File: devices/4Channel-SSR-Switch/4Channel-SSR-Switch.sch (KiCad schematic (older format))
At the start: 23 parts, among them J1 RJ45, J2 RJ45, P1 CONN_02X05, P2 CONN_01X05, P3 CONN_01X05, P4 CONN_01X05, P6 CONN_01X05, U1 LP2950, U2 STM32F030R8, U3 G3MB_SSR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

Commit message: Big cleanup/upgrade of Kicad files
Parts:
- added D1: SMF05C, SMF05C:SC70-6, symbol SMF05C:SMF05C
- added ZD1: DS9503, DS9503:TSOC6, symbol DS9503:DS9503
- C1: symbol CP -> 4Channel-SSR-Switch-rescue:CP
- C2, C3, C4, C5: symbol C -> 4Channel-SSR-Switch-rescue:C
- J1, J2: symbol RJ45 -> 4Channel-SSR-Switch-rescue:RJ45
- P1: symbol CONN_02X05 -> 4Channel-SSR-Switch-rescue:CONN_02X05
- P2, P3, P4, P6: symbol CONN_01X05 -> 4Channel-SSR-Switch-rescue:CONN_01X05
- R1: symbol R -> 4Channel-SSR-Switch-rescue:R
- RP1, RP2, RP3, RP4: symbol R_PACK4 -> 4Channel-SSR-Switch-rescue:R_PACK4
- U1: symbol LP2950 -> 4Channel-SSR-Switch-rescue:LP2950
- U2: symbol STM32F030R8 -> 4Channel-SSR-Switch-rescue:STM32F030R8
- U3, U4, U5, U6: symbol G3MB_SSR -> 4Channel-SSR-Switch-rescue:G3MB_SSR
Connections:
- net +5V: now also D1.1 (C1), D1.3 (C2), D1.4 (C3), D1.5 (C4), D1.6 (C5)
- net 1W-DATA: now also ZD1.1 (P$1); no longer J1.4, J2.4
- net GND: now also D1.2 (A), ZD1.2 (P$2); no longer J1.1, J1.3, J1.5, J1.8, J1.9 (SHIELD), J2.1, J2.3, J2.5, J2.8, J2.9 (SHIELD)
- new net: J1.1, J1.3, J1.5, J1.8, J1.9 (SHIELD), J2.1, J2.3, J2.5, J2.8, J2.9 (SHIELD), ZD1.5 (P$3)
- new net: J1.4, J2.4, ZD1.6 (P$4)

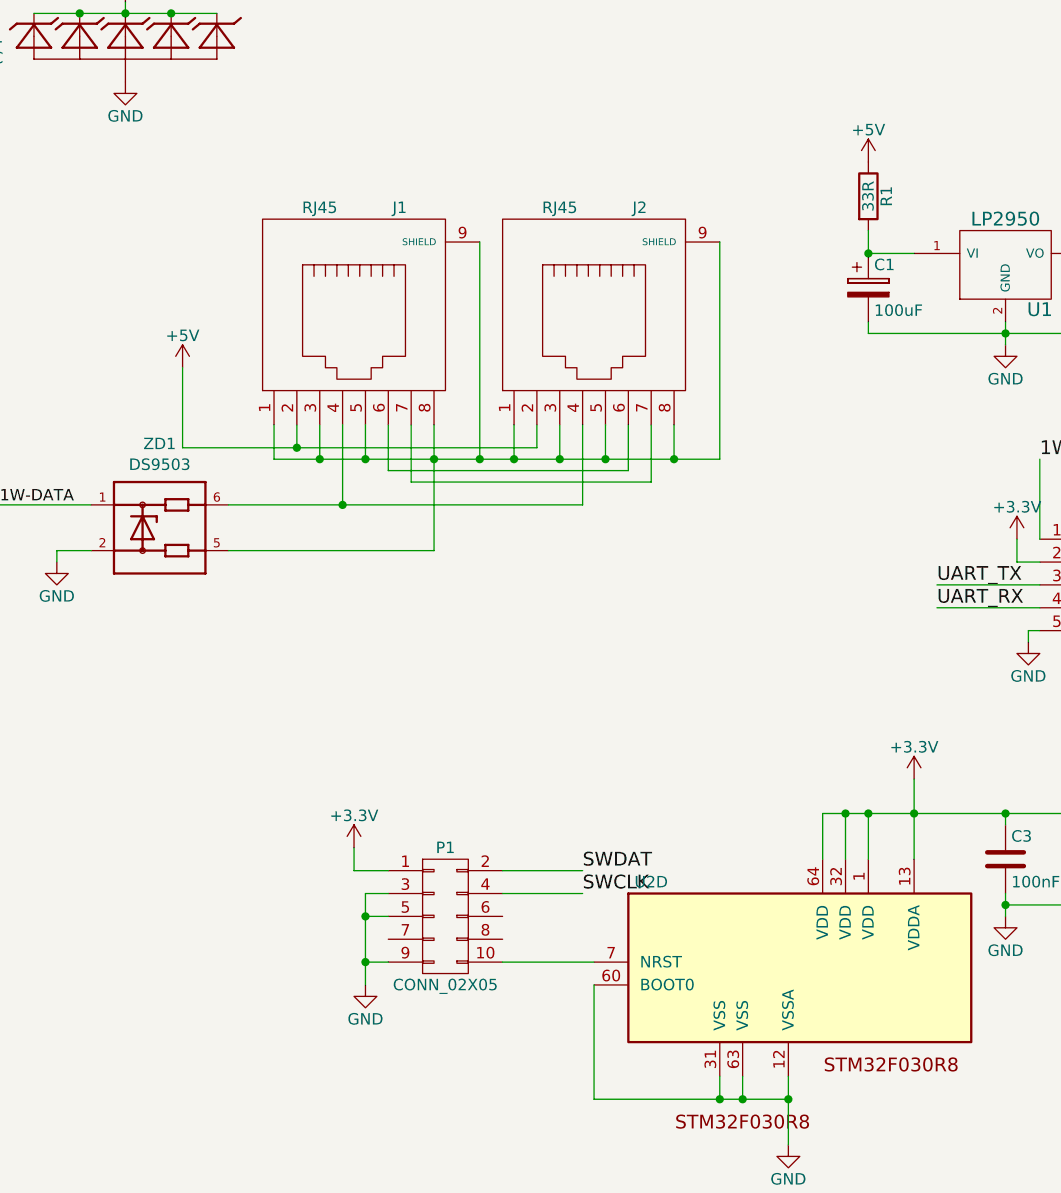
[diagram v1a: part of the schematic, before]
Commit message: Bump all active boards to Revision 1.2
- Remove dropping resistor from 5V power line
- Add pullup resistor to Reset line
- Add pin markings to STM32 chip footprint

Signed-off-by: Alastair D'Silva <alastair@d-silva.org>
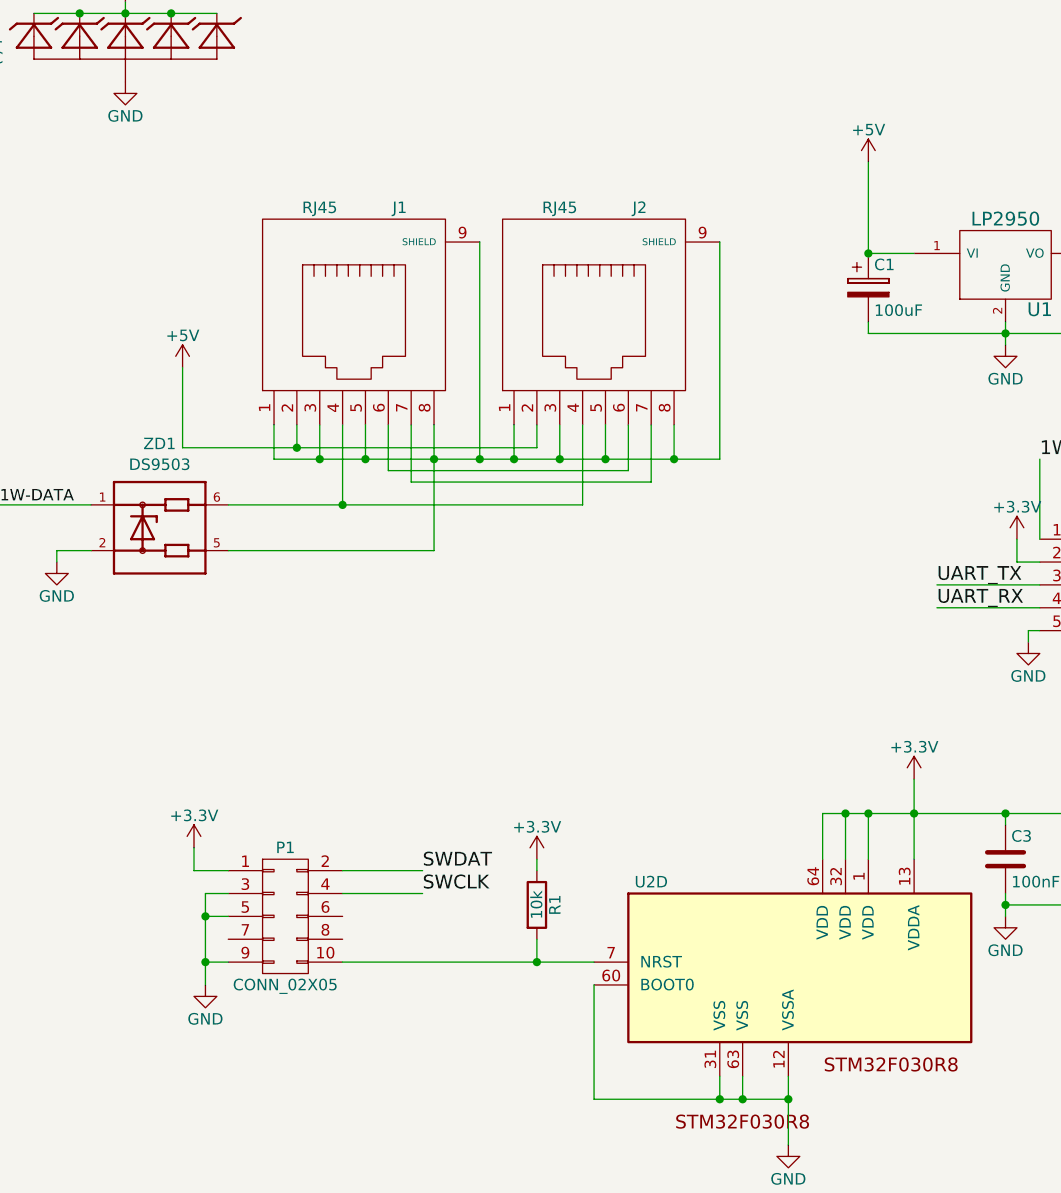
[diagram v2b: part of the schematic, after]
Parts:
- R1: value 33R -> 10k
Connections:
- net +3V3: now also R1.1
- net +5V: now also C1.1, U1.1 (VI); no longer R1.1
- net at P1.10 (P10), U2.7 (NRST): now also R1.2
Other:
- moved on the sheet: P1, R1
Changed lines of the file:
@@
 Sheet 1 1
 Title "4 Channel SSR Switch"
-Date "2018-10-30"
-Rev "1.0"
+Date "2018-12-23"
+Rev "1.2"
 Comp "Inferno Embedded"
 Comment1 "Licensed under the TAPR Open Hardware License (www.tapr.org/OHL)"
@@
 L 4Channel-SSR-Switch-rescue:CONN_02X05 P1
 U 1 1 58245605
-P 12450 8500
-F 0 "P1" H 12450 8800 50  0000 C CNN
-F 1 "CONN_02X05" H 12450 8200 50  0000 C CNN
-F 2 "Pin_Headers:Pin_Header_Straight_2x05_Pitch2.54mm_SMD" H 12450 7300 50  0001 C CNN
-F 3 "" H 12450 7300 50  0000 C CNN
-	1    12450 8500
+P 11750 8500
+F 0 "P1" H 11750 8800 50  0000 C CNN
+F 1 "CONN_02X05" H 11750 8200 50  0000 C CNN
+F 2 "Pin_Headers:Pin_Header_Straight_2x05_Pitch2.54mm_SMD" H 11750 7300 50  0001 C CNN
+F 3 "" H 11750 7300 50  0000 C CNN
+	1    11750 8500
 	1    0    0    -1
 $EndComp
@@
 L 4Channel-SSR-Switch-rescue:GND #PWR05
 U 1 1 58245733
-P 12100 8800
-F 0 "#PWR05" H 12100 8550 50  0001 C CNN
-F 1 "GND" H 12100 8650 50  0000 C CNN
-F 2 "" H 12100 8800 50  0000 C CNN
-F 3 "" H 12100 8800 50  0000 C CNN
-	1    12100 8800
+P 11400 8800
+F 0 "#PWR05" H 11400 8550 50  0001 C CNN
+F 1 "GND" H 11400 8650 50  0000 C CNN
+F 2 "" H 11400 8800 50  0000 C CNN
+F 3 "" H 11400 8800 50  0000 C CNN
+	1    11400 8800
 	1    0    0    -1
 $EndComp
@@
 F 3 "" H 5100 6850 50  0000 C CNN
 	5    1800 9350
-	1    0    0    -1
-$EndComp
-$Comp
-L 4Channel-SSR-Switch-rescue:R R1
-U 1 1 58B28CDC
-P 14300 5350
-F 0 "R1" V 14380 5350 50  0000 C CNN
-F 1 "33R" V 14300 5350 50  0000 C CNN
-F 2 "Resistors_SMD:R_0603" V 14230 5350 50  0001 C CNN
-F 3 "" H 14300 5350 50  0000 C CNN
-	1    14300 5350
 	1    0    0    -1
 $EndComp
@@
 	1    0    0    -1
 $EndComp
-Text Label 13050 8300 0    60   ~ 0
+Text Label 12350 8300 0    60   ~ 0
 SWDAT
-Text Label 13050 8400 0    60   ~ 0
+Text Label 12350 8400 0    60   ~ 0
 SWCLK
 Text Label 14600 7050 0    60   ~ 0
@@
 L 4Channel-SSR-Switch-rescue:+3.3V #PWR012
 U 1 1 58C3775D
-P 12050 8200
-F 0 "#PWR012" H 12050 8050 50  0001 C CNN
-F 1 "+3.3V" H 12050 8340 50  0000 C CNN
-F 2 "" H 12050 8200 50  0000 C CNN
-F 3 "" H 12050 8200 50  0000 C CNN
-	1    12050 8200
+P 11350 8200
+F 0 "#PWR012" H 11350 8050 50  0001 C CNN
+F 1 "+3.3V" H 11350 8340 50  0000 C CNN
+F 2 "" H 11350 8200 50  0000 C CNN
+F 3 "" H 11350 8200 50  0000 C CNN
+	1    11350 8200
 	1    0    0    -1
 $EndComp
@@
 Connection ~ 14200 8050
 Wire Wire Line
-	12050 8200 12050 8300
-Wire Wire Line
-	12050 8300 12200 8300
-Wire Wire Line
-	12200 8400 12100 8400
-Wire Wire Line
-	12100 8400 12100 8500
-Wire Wire Line
-	12200 8500 12100 8500
-Connection ~ 12100 8500
-Wire Wire Line
-	12200 8700 12100 8700
-Connection ~ 12100 8700
+	11350 8200 11350 8300
+Wire Wire Line
+	11350 8300 11500 8300
+Wire Wire Line
+	11500 8400 11400 8400
+Wire Wire Line
+	11400 8400 11400 8500
+Wire Wire Line
+	11500 8500 11400 8500
+Connection ~ 11400 8500
+Wire Wire Line
+	11500 8700 11400 8700
+Connection ~ 11400 8700
 Wire Wire Line
 	12000 6350 12000 6700
@@
 Wire Wire Line
 	14500 5600 14300 5600
-Wire Wire Line
-	14300 5600 14300 5500
 Wire Wire Line
 	14300 5900 14300 5950
@@
 	4600 6650 4950 6650
 Wire Wire Line
-	12700 8300 13050 8300
-Wire Wire Line
-	12700 8400 13050 8400
+	12000 8300 12350 8300
+Wire Wire Line
+	12000 8400 12350 8400
 Wire Wire Line
 	2800 9550 3050 9550
-Wire Wire Line
-	13100 8700 12700 8700
 Wire Wire Line
 	14500 800  14050 800
@@
 	14200 8050 14300 8050
 Wire Wire Line
-	12100 8500 12100 8700
-Wire Wire Line
-	12100 8700 12100 8800
+	11400 8500 11400 8700
+Wire Wire Line
+	11400 8700 11400 8800
 Wire Wire Line
 	14900 5950 15400 5950
@@
 Text Label 10500 6700 0    50   ~ 0
 1W-DATA
+$Comp
+L 4Channel-SSR-Switch-rescue:R R1
+U 1 1 58B28CDC
+P 12850 8450
+F 0 "R1" V 12930 8450 50  0000 C CNN
+F 1 "10k" V 12850 8450 50  0000 C CNN
+F 2 "Resistors_SMD:R_0603" V 12780 8450 50  0001 C CNN
+F 3 "" H 12850 8450 50  0000 C CNN
+	1    12850 8450
+	1    0    0    -1
+$EndComp
+Wire Wire Line
+	12000 8700 12850 8700
+Wire Wire Line
+	12850 8600 12850 8700
+Connection ~ 12850 8700
+Wire Wire Line
+	12850 8700 13100 8700
+$Comp
+L 4Channel-SSR-Switch-rescue:+3.3V #PWR?
+U 1 1 5C262187
+P 12850 8250
+F 0 "#PWR?" H 12850 8100 50  0001 C CNN
+F 1 "+3.3V" H 12850 8390 50  0000 C CNN
+F 2 "" H 12850 8250 50  0000 C CNN
+F 3 "" H 12850 8250 50  0000 C CNN
+	1    12850 8250
+	1    0    0    -1
+$EndComp
+Wire Wire Line
+	12850 8250 12850 8300
+Wire Wire Line
+	14300 5200 14300 5600
 $EndSCHEMATC
